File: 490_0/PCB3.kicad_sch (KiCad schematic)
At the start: 1 part, among them J6 Conn_01x08

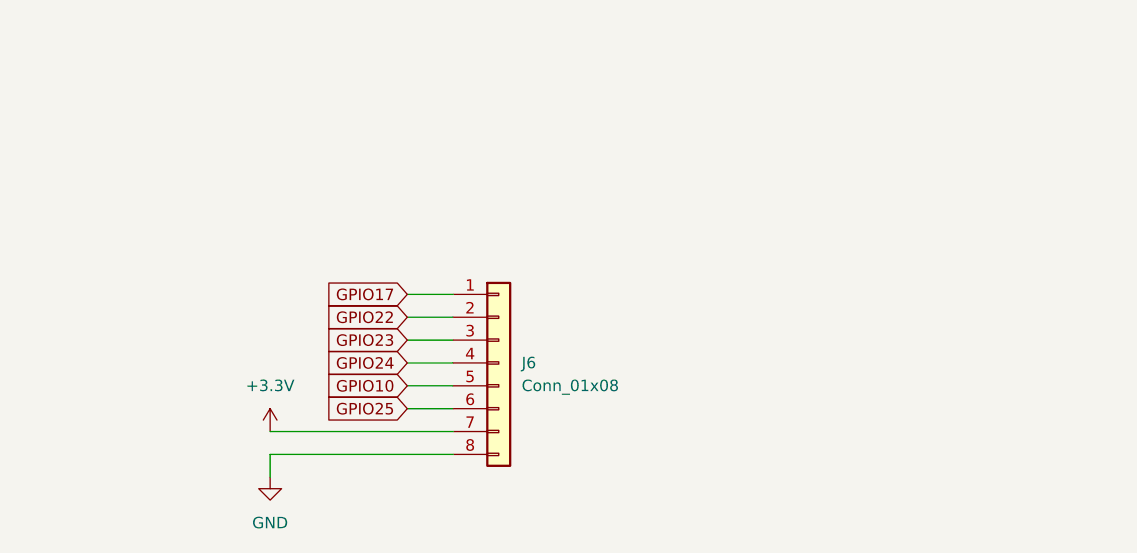
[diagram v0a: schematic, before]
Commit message: Schematic layout update
- applied hierarchical labels
- cleaned up the schematic
- finalized CM4 connections
- checked cm4 connections
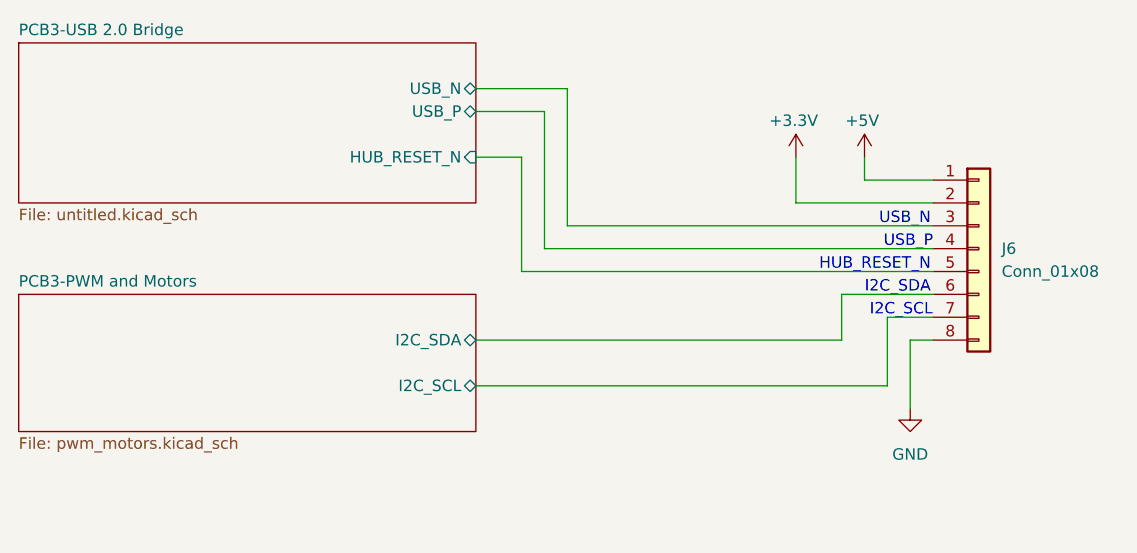
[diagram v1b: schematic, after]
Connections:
- net GPIO22 is gone; now on net +3.3V: J6.2 (Pin_2)
- net +3.3V: no longer J6.7 (Pin_7)
- net GPIO10 renamed PCB3-USB 2.0 Bridge/HUB_RESET_N
- net GPIO17 renamed +5V
- net GPIO23 renamed PCB3-USB 2.0 Bridge/USB_N
- net GPIO24 renamed PCB3-USB 2.0 Bridge/USB_P
- net GPIO25 renamed PCB3-PWM and Motors/I2C_SDA
- new net PCB3-PWM and Motors/I2C_SCL: J6.7 (Pin_7)
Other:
- added sheet PCB3-PWM and Motors (pwm_motors.kicad_sch)
- added sheet PCB3-USB 2.0 Bridge (untitled.kicad_sch)
- note added: "HUB_RESET_N"
- note added: "I2C_SCL"
- note added: "I2C_SDA"
- note added: "USB_N"
- note added: "USB_P"

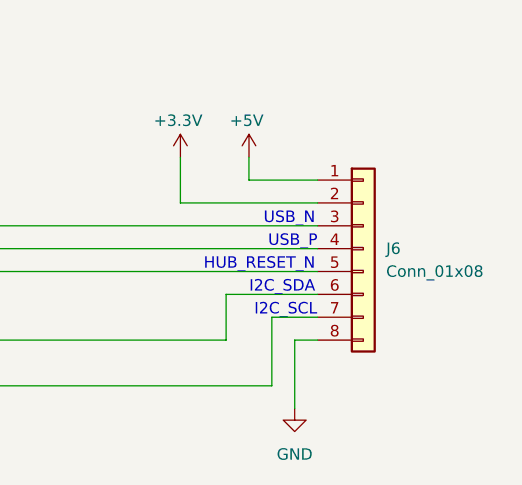
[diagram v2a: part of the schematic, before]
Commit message: Power + BOM update
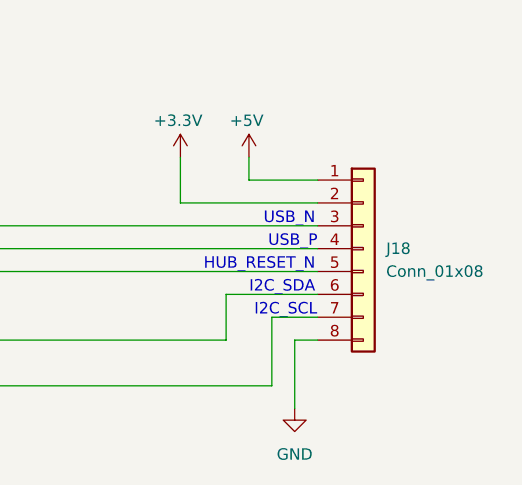
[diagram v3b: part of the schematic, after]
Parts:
- J18: renamed from J6; footprint 4ms_Connector:Pins_1x08_2.54mm_TH -> (none)
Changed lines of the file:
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@@
 		(on_board yes)
 		(dnp no)
-		(property "Reference" "#PWR016"
+		(property "Reference" "#PWR0105"
 			(at 185.42 72.39 0)
 			(effects
@@
 			(project "490_0"
 				(path "/365a82ed-827d-43e1-aa2f-b98221c4179c/a8971e06-9d2b-4df6-83ab-783791bb1c3f"
-					(reference "#PWR016")
+					(reference "#PWR0105")
 					(unit 1)
 				)
@@
 		(on_board yes)
 		(dnp no)
-		(property "Reference" "#PWR0144"
+		(property "Reference" "#PWR0104"
 			(at 177.8 72.39 0)
 			(effects
@@
 			(project "490_0"
 				(path "/365a82ed-827d-43e1-aa2f-b98221c4179c/a8971e06-9d2b-4df6-83ab-783791bb1c3f"
-					(reference "#PWR0144")
+					(reference "#PWR0104")
 					(unit 1)
 				)
@@
 		(dnp no)
 		(fields_autoplaced yes)
-		(property "Reference" "J6"
+		(property "Reference" "J18"
 			(at 200.66 78.7399 0)
 			(effects
@@
 			)
 		)
-		(property "Footprint" "4ms_Connector:Pins_1x08_2.54mm_TH"
+		(property "Footprint" ""
 			(at 198.12 66.675 0)
 			(effects
@@
 			(project ""
 				(path "/365a82ed-827d-43e1-aa2f-b98221c4179c/a8971e06-9d2b-4df6-83ab-783791bb1c3f"
-					(reference "J6")
+					(reference "J18")
 					(unit 1)
 				)
@@
 		(dnp no)
 		(fields_autoplaced yes)
-		(property "Reference" "#PWR0143"
+		(property "Reference" "#PWR0106"
 			(at 190.5 102.87 0)
 			(effects
@@
 			(project "490_0"
 				(path "/365a82ed-827d-43e1-aa2f-b98221c4179c/a8971e06-9d2b-4df6-83ab-783791bb1c3f"
-					(reference "#PWR0143")
-					(unit 1)
-				)
+					(reference "#PWR0106")
+					(unit 1)
+				)

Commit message: finished BOM
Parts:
- J18: Digikey Link (none) -> https://www.digikey.ca/en/products/detail/jst-sales-america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; Manufacturer (none) -> JST Sales America Inc.; Manufacturer Part (none) -> S8B-XH-A; Price (none) -> 0.33; Supplier (none) -> DigiKey; Supplier P/N (none) -> 455-S8B-XH-A-ND; Type (none) -> Through Hole; Unit (none) -> pcs
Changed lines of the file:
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@@
 			)
 		)
-		(property "Datasheet" ""
+		(property "Datasheet" "kicad-embed://B3B-XH-A.pdf"
 			(at 198.12 73.66 0)
 			(effects
@@
 			)
 		)
-		(property "Description" "HEADER 1x8 MALE PINS 0.100” 180deg"
+		(property "Description" "CONN HEADER R/A 8POS 2.5MM"
 			(at 198.12 78.74 0)
 			(effects
@@
 				(hide yes)
 			)
+		)
+		(property "Digikey Link" "https://www.digikey.ca/en/products/detail/jst-sales-america-inc/S8B-XH-A/1651023"
+			(at 198.12 78.74 0)
+			(effects
+				(font
+					(size 1.27 1.27)
+				)
+				(hide yes)
+			)
+		)
+		(property "Manufacturer" "JST Sales America Inc."
+			(at 198.12 78.74 0)
+			(effects
+				(font
+					(size 1.27 1.27)
+				)
+				(hide yes)
+			)
+		)
+		(property "Manufacturer Part" "S8B-XH-A"
+			(at 198.12 78.74 0)
+			(effects
+				(font
+					(size 1.27 1.27)
+				)
+				(hide yes)
+			)
+		)
+		(property "Price" "0.33"
+			(at 198.12 78.74 0)
+			(effects
+				(font
+					(size 1.27 1.27)
+				)
+				(hide yes)
+			)
+		)
+		(property "Supplier" "DigiKey"
+			(at 198.12 78.74 0)
+			(effects
+				(font
+					(size 1.27 1.27)
+				)
+				(hide yes)
+			)
+		)
+		(property "Supplier P/N" "455-S8B-XH-A-ND"
+			(at 198.12 78.74 0)
+			(effects
+				(font
+					(size 1.27 1.27)
+				)
+				(hide yes)
+			)
+		)
+		(property "Type" "Through Hole"
+			(at 198.12 78.74 0)
+			(effects
+				(font
+					(size 1.27 1.27)
+				)
+				(hide yes)
+			)
+		)
+		(property "Unit" "pcs"
+			(at 198.12 78.74 0)
+			(effects
+				(font
+					(size 1.27 1.27)
+				)
+				(hide yes)
+			)
+		)
+		(property "Voltage Raing" ""
+			(at 198.12 78.74 0)
+			(effects
+				(font
+					(size 1.27 1.27)
+				)
+				(hide yes)
+			)
+		)
+		(property "Voltage Rating" ""
+			(at 198.12 78.74 0)
+			(effects
+				(font
+					(size 1.27 1.27)
+				)
+				(hide yes)
+			)

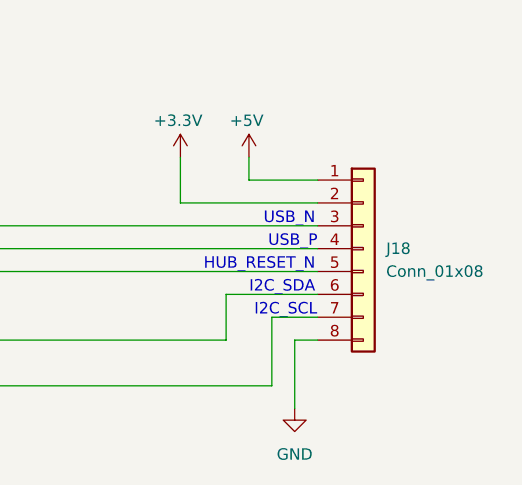
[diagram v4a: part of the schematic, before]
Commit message: Implemented Dmitry comments
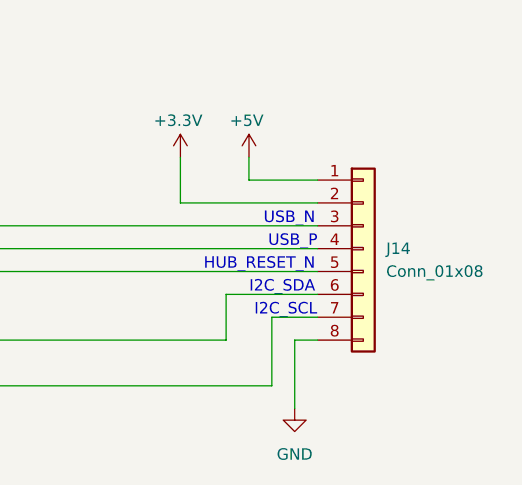
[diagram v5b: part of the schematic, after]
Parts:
- renumbered J18 to J14
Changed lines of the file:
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@@
 		(on_board yes)
 		(dnp no)
-		(property "Reference" "#PWR0105"
+		(property "Reference" "#PWR096"
 			(at 185.42 72.39 0)
 			(effects
@@
 			(project "490_0"
 				(path "/365a82ed-827d-43e1-aa2f-b98221c4179c/a8971e06-9d2b-4df6-83ab-783791bb1c3f"
-					(reference "#PWR0105")
+					(reference "#PWR096")
 					(unit 1)
 				)
@@
 		(on_board yes)
 		(dnp no)
-		(property "Reference" "#PWR0104"
+		(property "Reference" "#PWR095"
 			(at 177.8 72.39 0)
 			(effects
@@
 			(project "490_0"
 				(path "/365a82ed-827d-43e1-aa2f-b98221c4179c/a8971e06-9d2b-4df6-83ab-783791bb1c3f"
-					(reference "#PWR0104")
+					(reference "#PWR095")
 					(unit 1)
 				)
@@
 		(dnp no)
 		(fields_autoplaced yes)
-		(property "Reference" "J18"
+		(property "Reference" "J14"
 			(at 200.66 78.7399 0)
 			(effects
@@
 			(project ""
 				(path "/365a82ed-827d-43e1-aa2f-b98221c4179c/a8971e06-9d2b-4df6-83ab-783791bb1c3f"
-					(reference "J18")
+					(reference "J14")
 					(unit 1)
 				)
@@
 		(dnp no)
 		(fields_autoplaced yes)
-		(property "Reference" "#PWR0106"
+		(property "Reference" "#PWR097"
 			(at 190.5 102.87 0)
 			(effects
@@
 			(project "490_0"
 				(path "/365a82ed-827d-43e1-aa2f-b98221c4179c/a8971e06-9d2b-4df6-83ab-783791bb1c3f"
-					(reference "#PWR0106")
+					(reference "#PWR097")
 					(unit 1)
 				)

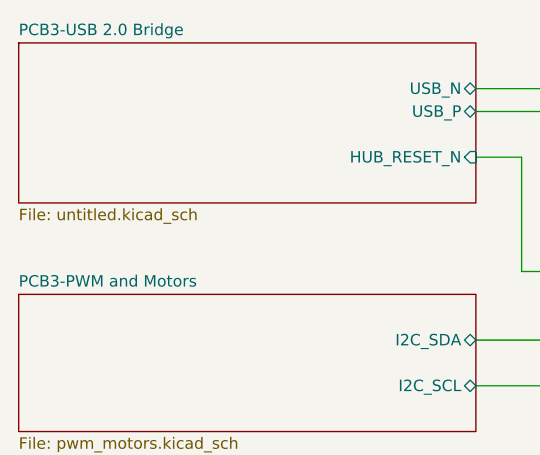
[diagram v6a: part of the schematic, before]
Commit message: Implemented suggestions
notes on schematics:
Overall: Schematics needs to be improved, more compact and cleaner
=========================
I) on root page (page 1):
overall: needs a bit of clean up of the diagram

1. the diagram shows pcb3 and pcb1, but no pcb2, it is probably outdated and therefore might have errors in it, fix it to the latest version and rename things to reflect what it actually is. Also try to clean it up a bit
2. The PCB-3 seem to have the cameras directly connected to the usb hub, how will this be connected? with connectors? if so add them to the diagram, if it's with wires soldered directly to the pcb, try to make note of it for clarity
4. for some reason your TOF is above PCB-3 but is only connected to PCB1, will the TOF be on the glasses, or will you be moving this to the main board? maybe have TOF on the chest for depth, and 2 cameras on glasses for vision, it will also reduce length of cable, which is ideal, i don't think it will work if you run it from the glasses to pcb1 though.
I know, this is a problem, we discussed the chest thing, the problem is the length of the cable but also the haptic feedback is weird if they turn their head.
5. Rename PCB1/PCB3 to PCB1 (chest) PCB3 (glasses) for clarity. Also i don't think (mayeb i'm wrong) that the 5 conected buttons should be on a bus, a bus implies that multiple devices communicate on the same single line. You're using individual lines for each to individual gpio, no?

=========================
II) on PCB-3 usb 2.0 bridge page (page 10)
overall: check datasheet and make sure you've done the connection right and values are selected properly, with the chip data lines properly pulled up/down whether externally or internally. This is important

1. C3/C11 are the input capacitors to U2/u3 TPS553DBVR, datasheet says 100nF, you used 10uF, why? stick to 100nF
2. you seem to have implemented one of /Uthe typical application circuit, look at the others. You have on page 21 of datasheet an auto-retry wi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
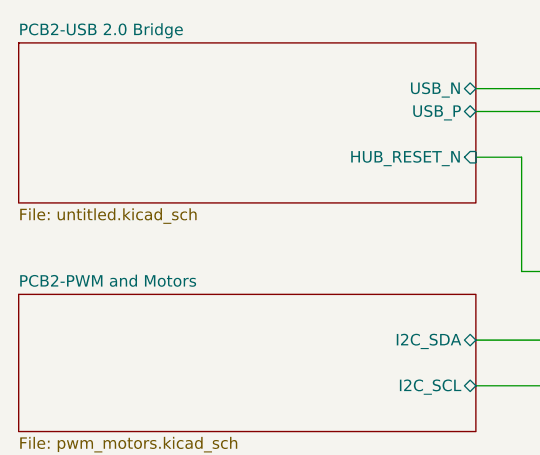
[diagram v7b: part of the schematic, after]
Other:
- sheet PCB3-PWM and Motors renamed PCB2-PWM and Motors
- sheet PCB3-USB 2.0 Bridge renamed PCB2-USB 2.0 Bridge
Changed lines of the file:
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@@
 			(color 0 0 0 0.0000)
 		)
-		(property "Sheetname" "PCB3-USB 2.0 Bridge"
+		(property "Sheetname" "PCB2-USB 2.0 Bridge"
 			(at 91.44 55.1684 0)
 			(effects
@@
 			(color 0 0 0 0.0000)
 		)
-		(property "Sheetname" "PCB3-PWM and Motors"
+		(property "Sheetname" "PCB2-PWM and Motors"
 			(at 91.44 83.1084 0)
 			(effects

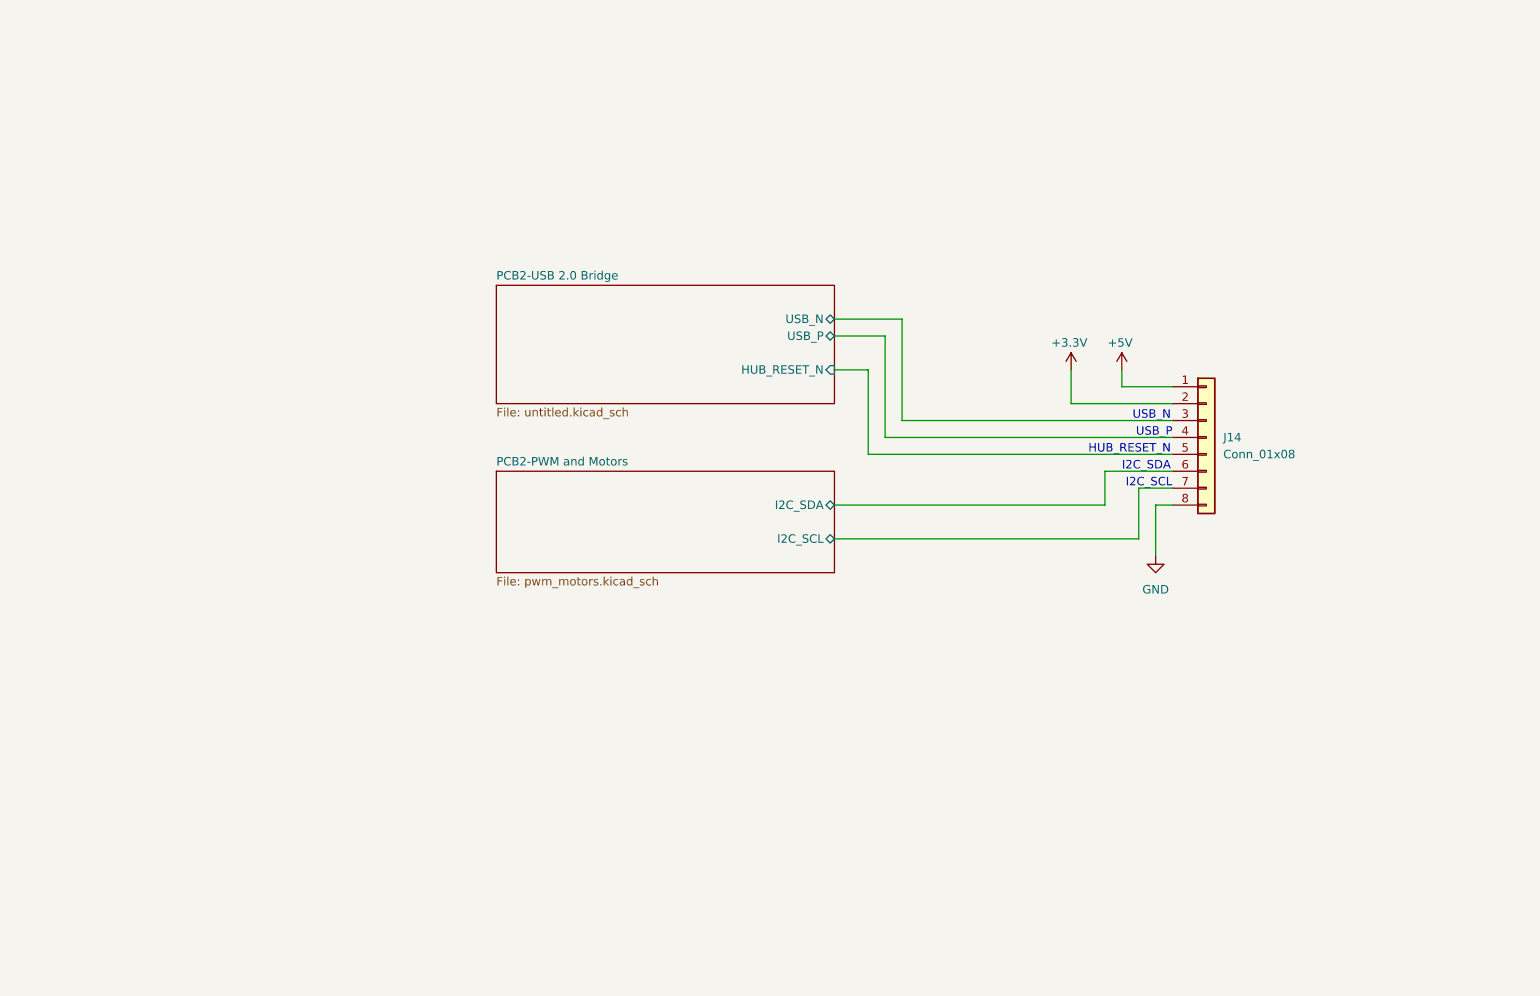
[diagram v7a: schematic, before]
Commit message: FFC to HDMI change
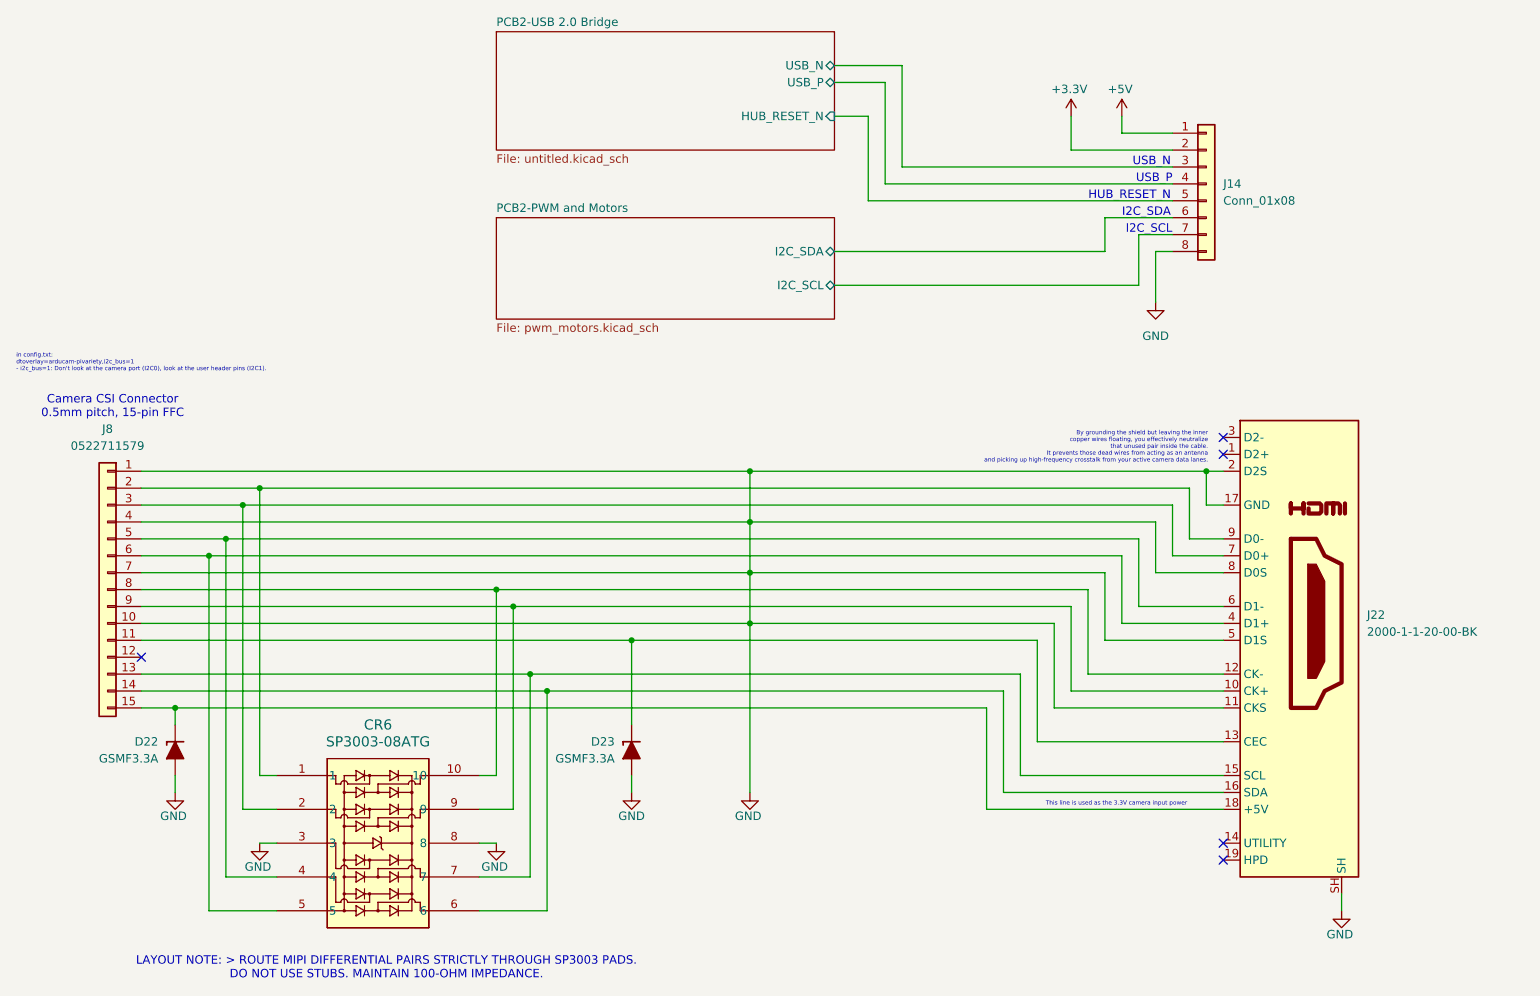
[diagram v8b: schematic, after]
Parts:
- added CR6: SP3003-08ATG, MSOP10_MO-187_LTF, symbol capstone_parts:SP3003-08ATG
- added D22, D23: GSMF3.3A, PCM_Diode_SMD_AKL:D_SOD-123F, symbol PCM_Diode_TVS_AKL:SMF5.0A
- added J22: 2000-1-1-20-00-BK, symbol Connector:HDMI_A
- added J8: 0522711579, symbol Connector_Generic:Conn_01x15
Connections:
- net GND: now also CR6.3, CR6.8, D22.2 (A), D23.2 (A), J22.11 (CKS), J22.17 (GND), J22.2 (D2S), J22.5 (D1S), J22.8 (D0S), J22.SH, J8.1 (Pin_1), J8.10 (Pin_10), J8.4 (Pin_4), J8.7 (Pin_7)
- new net: D23.1 (K), J22.13 (CEC), J8.11 (Pin_11)
- new net: CR6.7, J22.15 (SCL), J8.13 (Pin_13)
- new net: CR6.6, J22.16 (SDA), J8.14 (Pin_14)
- new net: D22.1 (K), J22.18 (+5V), J8.15 (Pin_15)
- new net: CR6.1, J22.9 (D0-), J8.2 (Pin_2)
- new net: CR6.2, J22.7 (D0+), J8.3 (Pin_3)
- new net: CR6.4, J22.6 (D1-), J8.5 (Pin_5)
- new net: CR6.5, J22.4 (D1+), J8.6 (Pin_6)
- new net: CR6.10, J22.12 (CK-), J8.8 (Pin_8)
- new net: CR6.9, J22.10 (CK+), J8.9 (Pin_9)
- no-connect marks 0 -> 5
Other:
- note added: "By grounding the shield but leaving the inner copper wires floating, you effectively neutralize that unused pair inside the cable. It prevents those dead wires from acting as an antenna and picking up high-frequency crosstalk from your active camera data lanes."
- note added: "Camera CSI Connector 0.5mm pitch, 15-pin FFC"
- note added: "LAYOUT NOTE: > ROUTE MIPI DIFFERENTIAL PAIRS STRICTLY THROUGH SP3003 PADS. DO NOT USE STUBS. MAINTAIN 100-OHM IMPEDANCE."
- note added: "This line is used as the 3.3V camera input power"
- note added: "in config.txt: dtoverlay=arducam-pivariety,i2c_bus=1 - i2c_bus=1: Don't look at the camera port (I2C0), look at the user header pins (I2C1)."
- moved on the sheet: J14
